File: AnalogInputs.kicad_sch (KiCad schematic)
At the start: 44 parts, among them U34 LMV321, U35 LMV321, U36 LMV321, U37 LMV321, U38 LMV321, U39 LMV321, U40 LMV321, U41 LMV321

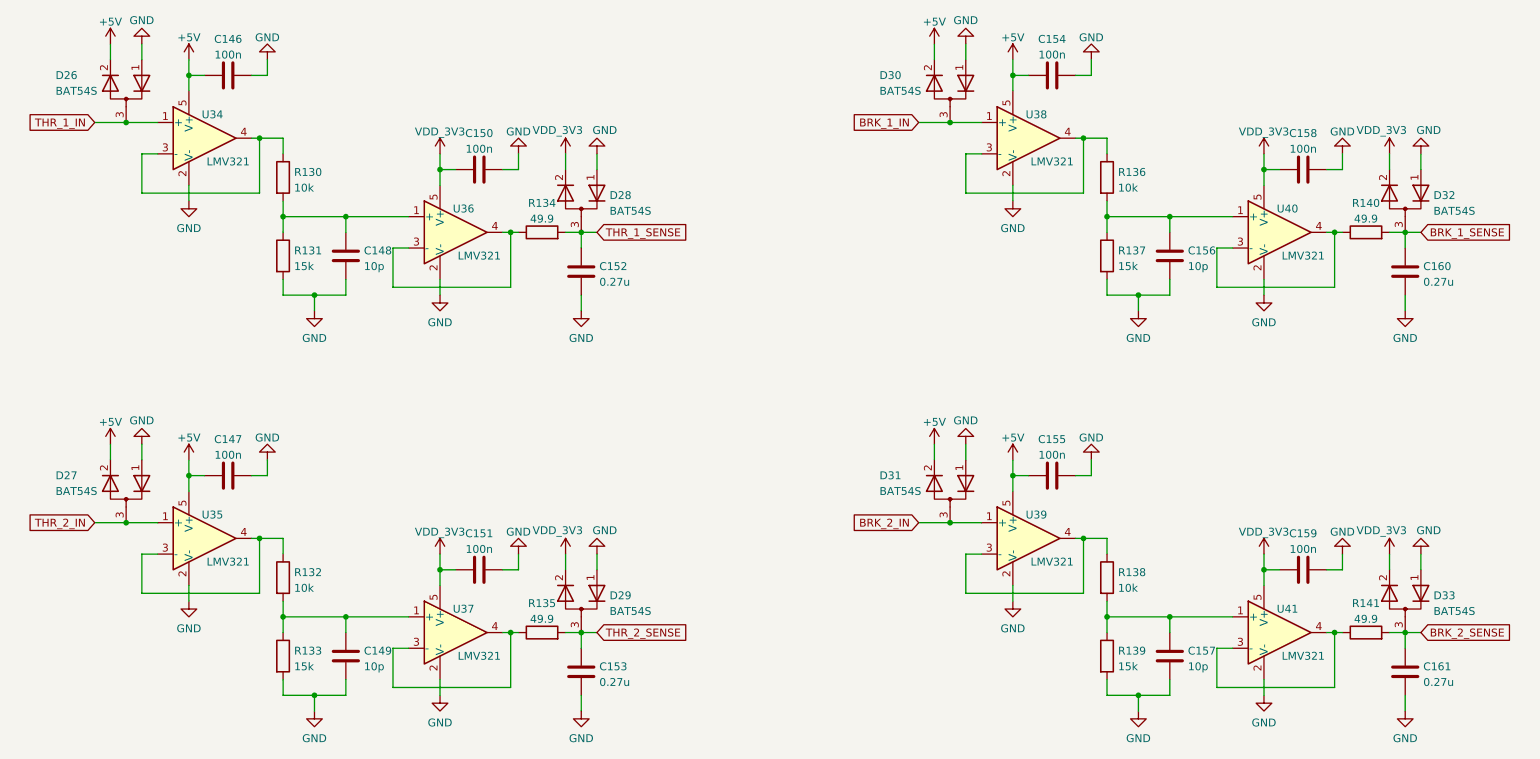
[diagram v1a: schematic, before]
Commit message: Изменения в схеме: поменял направление меток
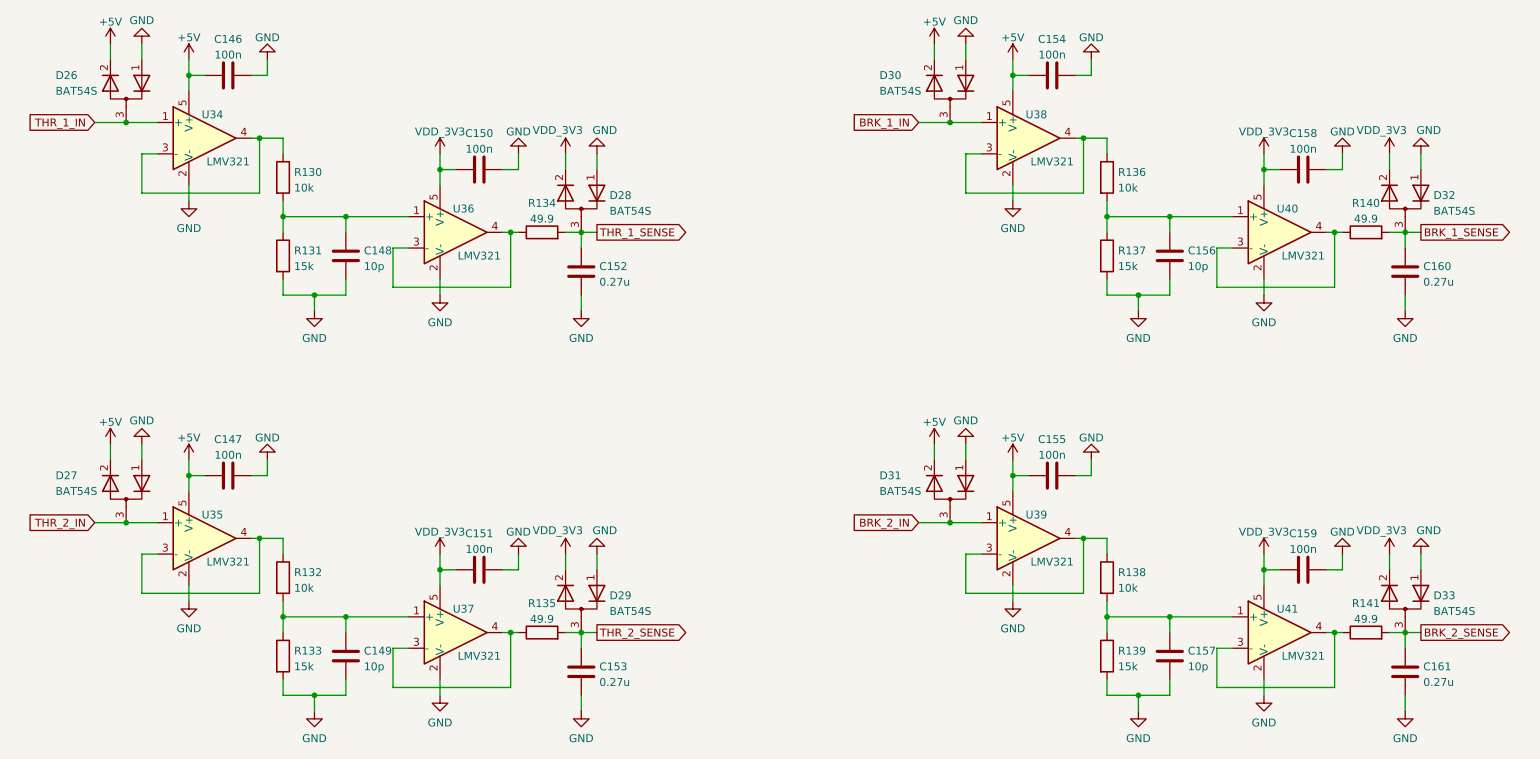
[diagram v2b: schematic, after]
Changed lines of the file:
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@@
 	)
 	(global_label "BRK_1_SENSE"
-		(shape input)
+		(shape output)
 		(at 273.05 62.23 0)
 		(fields_autoplaced yes)
@@
 		)
 		(property "Intersheetrefs" "${INTERSHEET_REFS}"
-			(at 288.4655 62.1506 0)
+			(at 289.0374 62.23 0)
 			(effects
 				(font
@@
 	)
 	(global_label "THR_1_SENSE"
-		(shape input)
+		(shape output)
 		(at 139.7 62.23 0)
 		(fields_autoplaced yes)
@@
 		)
 		(property "Intersheetrefs" "${INTERSHEET_REFS}"
-			(at 154.8736 62.1506 0)
+			(at 155.4455 62.23 0)
 			(effects
 				(font
@@
 	)
 	(global_label "BRK_2_SENSE"
-		(shape input)
+		(shape output)
 		(at 273.05 127 0)
 		(fields_autoplaced yes)
@@
 		)
 		(property "Intersheetrefs" "${INTERSHEET_REFS}"
-			(at 288.4655 126.9206 0)
+			(at 289.0374 127 0)
 			(effects
 				(font
@@
 	)
 	(global_label "THR_2_SENSE"
-		(shape input)
+		(shape output)
 		(at 139.7 127 0)
 		(fields_autoplaced yes)
@@
 		)
 		(property "Intersheetrefs" "${INTERSHEET_REFS}"
-			(at 154.8736 126.9206 0)
+			(at 155.4455 127 0)
 			(effects
 				(font
